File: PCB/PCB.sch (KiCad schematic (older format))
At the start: 32 parts, among them J1 USB_B, U1 ESP32-WROOM-32, X1 12MHz

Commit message: LED indicator #4
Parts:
- added Power, RXD, TXD, signal: LED_R, symbol Device:LED
- added R6, R7, R8, R9: 1k, Mlab_R:SMD-1206, symbol Device:R_Small
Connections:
- net +3V3: now also R6.2, R7.2, R8.2
- net GND: now also Power.1 (K), signal.1 (K)
- net RXD: now also RXD.1 (K)
- net TXD: now also TXD.1 (K)
- net s_LED: now reaches U1.8 (IO32)
- net s_LED: now also R9.2
- new net: R6.1, RXD.2 (A)
- new net: R7.1, TXD.2 (A)
- new net: Power.2 (A), R8.1
- new net: R9.1, signal.2 (A)
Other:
- note added: "LED"

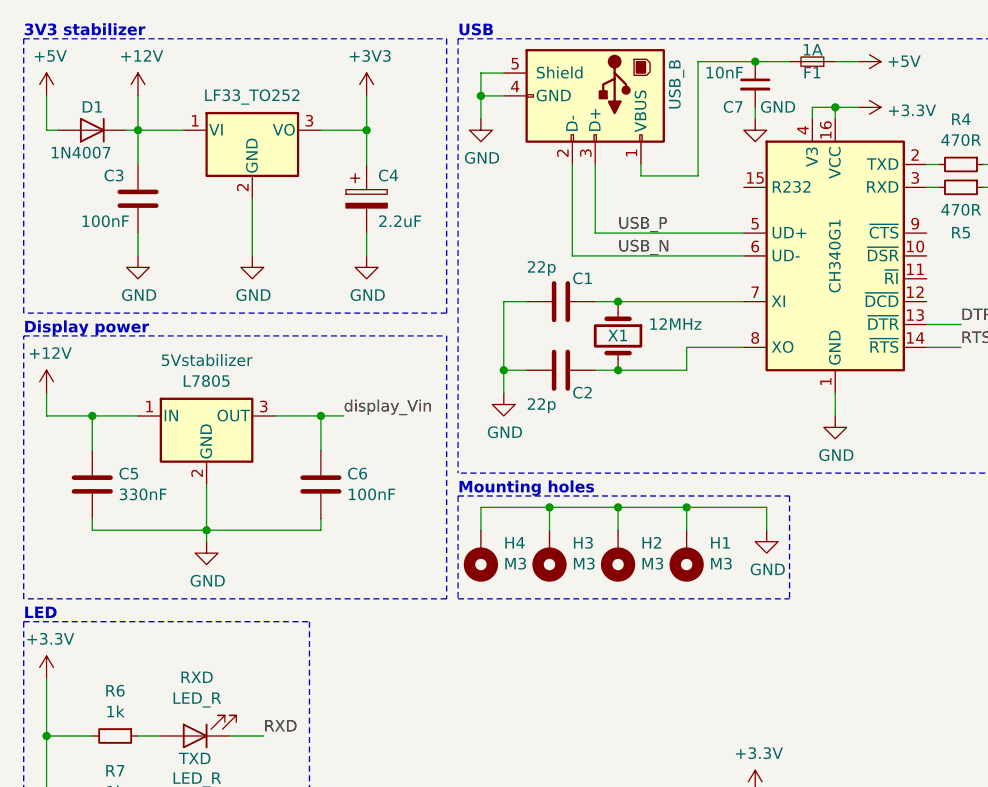
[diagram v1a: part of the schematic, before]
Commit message: schema update #4
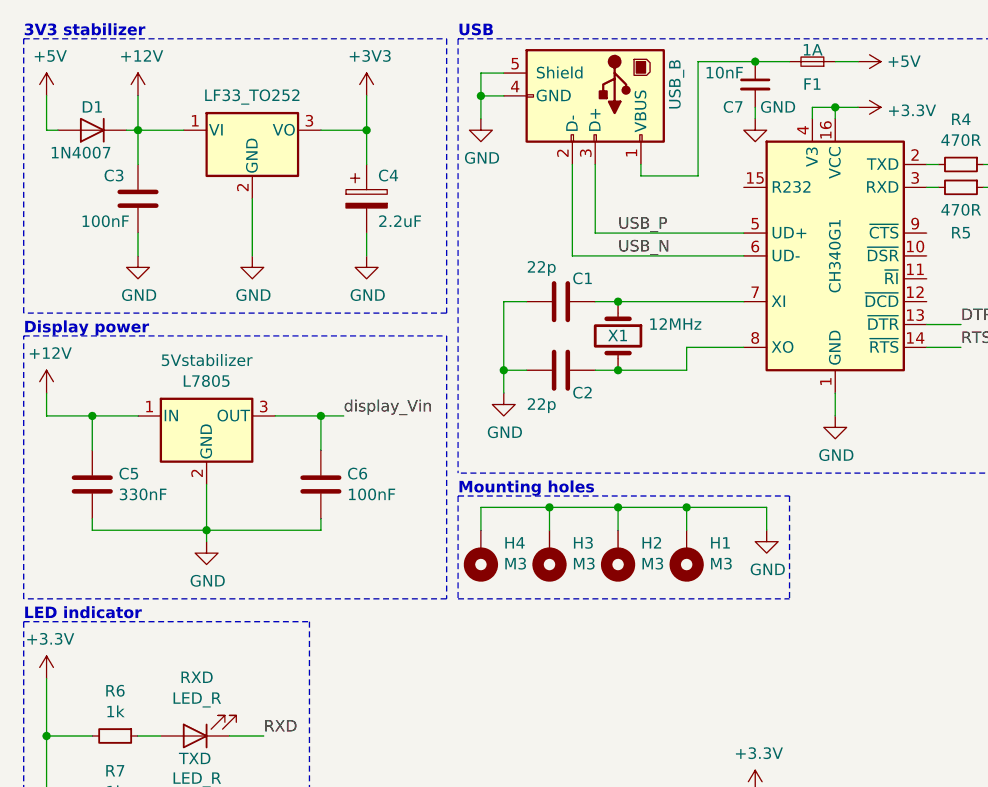
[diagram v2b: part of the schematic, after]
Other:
- note added: "LED indicator"
- note removed: "LED"
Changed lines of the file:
@@
 U 1 1 5DF6469B
 P 4000 700
-F 0 "F1" H 4000 750 50  0000 C CNN
+F 0 "F1" H 4000 800 50  0000 C CNN
 F 1 "1A" H 4000 650 50  0000 C CNN
 F 2 "Fuse:Fuse_1812_4532Metric_Pad1.30x3.40mm_HandSolder" H 4000 700 50  0001 C CNN
@@
 	550  5150 550  3150
 Text Notes 550  3150 0    50   ~ 10
-LED
+LED indicator
 $EndSCHEMATC

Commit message: reset circuit update
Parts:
- added MODE, RESET: SW_Push, symbol Switch:SW_Push
- added Q1, Q2: S8050, TO_SOT_Packages_SMD:SOT-23, symbol Transistor_BJT:S8050
- added R10, R11: 12k, symbol Device:R_Small
- added R12, R13: 10k, symbol Device:R_Small
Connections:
- net +3V3: now also R12.1, R13.1
- net GND: now also MODE.2, RESET.2
- net DTR: no longer names the net of CH340G1.13 (~DTR)
- net DTR: now also Q2.1 (E), R10.2; no longer U1.25 (IO0)
- net RTS: no longer names the net of CH340G1.14 (~RTS)
- net RTS: now also Q1.1 (E), R11.2; no longer U1.3 (EN)
- new net: Q1.2 (B), R10.1
- new net: Q2.2 (B), R11.1
- new net EN: Q1.3 (C), R12.2, RESET.1, U1.3 (EN)
- new net IO_0: MODE.1, Q2.3 (C), R13.2, U1.25 (IO0)
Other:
- note added: "Buttons"
- moved on the sheet: C1, C2, C7, CH340G1, D2, F1, H1, H2, H3, H4, I2C, NEXTION_UART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

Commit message: logo added #4
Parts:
- MODE, RESET: footprint (none) -> Buttons_Switches_SMD:SW_SPST_KMR2
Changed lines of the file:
@@
 F 0 "RESET" H 1050 6493 50  0000 C CNN
 F 1 "SW_Push" H 1050 6494 50  0001 C CNN
-F 2 "" H 1050 6500 50  0001 C CNN
+F 2 "Buttons_Switches_SMD:SW_SPST_KMR2" H 1050 6500 50  0001 C CNN
 F 3 "~" H 1050 6500 50  0001 C CNN
 	1    1050 6300
@@
 F 0 "MODE" H 1050 6793 50  0000 C CNN
 F 1 "SW_Push" H 1050 6794 50  0001 C CNN
-F 2 "" H 1050 6800 50  0001 C CNN
+F 2 "Buttons_Switches_SMD:SW_SPST_KMR2" H 1050 6800 50  0001 C CNN
 F 3 "~" H 1050 6800 50  0001 C CNN
 	1    1050 6600

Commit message: mosfet added #4
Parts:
- added P3A+, P3A-, P3B+, P3B-: WAGO256, Mlab_CON:WAGO256, symbol Connector_Generic:Conn_01x01
- added peltier3A, peltier3B: IRLR2905, Package_TO_SOT_SMD:TO-252-2_TabPin1, symbol Transistor_FET:IRLZ44N
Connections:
- net GND: now also P3A-.1 (Pin_1), P3B-.1 (Pin_1), peltier3A.3 (S), peltier3B.3 (S)
- net P3A: now reaches U1.30 (IO18)
- net P3A: now also peltier3A.1 (G)
- net P3B: now reaches U1.31 (IO19)
- net P3B: now also peltier3B.1 (G)
- new net: P3A+.1 (Pin_1), peltier3A.2 (D)
- new net: P3B+.1 (Pin_1), peltier3B.2 (D)
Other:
- note added: "3V peltiers"
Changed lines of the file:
@@
 Text Notes 550  6050 0    50   ~ 10
 Buttons
+$Comp
+L Transistor_FET:IRLZ44N peltier3A
+U 1 1 5DFD1541
+P 10200 4600
+F 0 "peltier3A" H 10406 4646 50  0000 L CNN
+F 1 "IRLR2905" H 10406 4555 50  0000 L CNN
+F 2 "Package_TO_SOT_SMD:TO-252-2_TabPin1" H 10450 4525 50  0001 L CIN
+F 3 "http://www.irf.com/product-info/datasheets/data/irlz44n.pdf" H 10200 4600 50  0001 L CNN
+	1    10200 4600
+	1    0    0    -1
+$EndComp
+$Comp
+L Connector_Generic:Conn_01x01 P3A+
+U 1 1 5DFED397
+P 10500 4300
+F 0 "P3A+" H 10580 4342 50  0000 L CNN
+F 1 "WAGO256" H 10580 4251 50  0000 L CNN
+F 2 "Mlab_CON:WAGO256" H 10500 4300 50  0001 C CNN
+F 3 "~" H 10500 4300 50  0001 C CNN
+	1    10500 4300
+	1    0    0    -1
+$EndComp
+$Comp
+L Connector_Generic:Conn_01x01 P3A-
+U 1 1 5DFF358D
+P 10500 4900
+F 0 "P3A-" H 10580 4942 50  0000 L CNN
+F 1 "WAGO256" H 10580 4851 50  0000 L CNN
+F 2 "Mlab_CON:WAGO256" H 10500 4900 50  0001 C CNN
+F 3 "~" H 10500 4900 50  0001 C CNN
+	1    10500 4900
+	1    0    0    -1
+$EndComp
+$Comp
+L power:GND #PWR?
+U 1 1 5E01ED3C
+P 10300 5000
+F 0 "#PWR?" H 10300 4750 50  0001 C CNN
+F 1 "GND" H 10305 4827 50  0000 C CNN
+F 2 "" H 10300 5000 50  0001 C CNN
+F 3 "" H 10300 5000 50  0001 C CNN
+	1    10300 5000
+	1    0    0    -1
+$EndComp
+Wire Wire Line
+	10300 4800 10300 4900
+Connection ~ 10300 4900
+Wire Wire Line
+	10300 4900 10300 5000
+Wire Wire Line
+	10300 4300 10300 4400
+Wire Wire Line
+	10000 4600 9950 4600
+Wire Wire Line
+	4350 5450 4500 5450
+Text Label 9950 4600 2    50   ~ 0
+P3A
+Text Label 4500 5450 0    50   ~ 0
+P3A
+$Comp
+L Transistor_FET:IRLZ44N peltier3B
+U 1 1 5E0B6BCD
+P 10200 5650
+F 0 "peltier3B" H 10406 5696 50  0000 L CNN
+F 1 "IRLR2905" H 10406 5605 50  0000 L CNN
+F 2 "Package_TO_SOT_SMD:TO-252-2_TabPin1" H 10450 5575 50  0001 L CIN
+F 3 "http://www.irf.com/product-info/datasheets/data/irlz44n.pdf" H 10200 5650 50  0001 L CNN
+	1    10200 5650
+	1    0    0    -1
+$EndComp
+$Comp
+L Connector_Generic:Conn_01x01 P3B+
+U 1 1 5E0B6BD7
+P 10500 5350
+F 0 "P3B+" H 10580 5392 50  0000 L CNN
+F 1 "WAGO256" H 10580 5301 50  0000 L CNN
+F 2 "Mlab_CON:WAGO256" H 10500 5350 50  0001 C CNN
+F 3 "~" H 10500 5350 50  0001 C CNN
+	1    10500 5350
+	1    0    0    -1
+$EndComp
+$Comp
+L Connector_Generic:Conn_01x01 P3B-
+U 1 1 5E0B6BE1
+P 10500 5950
+F 0 "P3B-" H 10580 5992 50  0000 L CNN
+F 1 "WAGO256" H 10580 5901 50  0000 L CNN
+F 2 "Mlab_CON:WAGO256" H 10500 5950 50  0001 C CNN
+F 3 "~" H 10500 5950 50  0001 C CNN
+	1    10500 5950
+	1    0    0    -1
+$EndComp
+$Comp
+L power:GND #PWR?
+U 1 1 5E0B6BEB
+P 10300 6050
+F 0 "#PWR?" H 10300 5800 50  0001 C CNN
+F 1 "GND" H 10305 5877 50  0000 C CNN
+F 2 "" H 10300 6050 50  0001 C CNN
+F 3 "" H 10300 6050 50  0001 C CNN
+	1    10300 6050
+	1    0    0    -1
+$EndComp
+Wire Wire Line
+	10300 5850 10300 5950
+Connection ~ 10300 5950
+Wire Wire Line
+	10300 5950 10300 6050
+Wire Wire Line
+	10300 5350 10300 5450
+Wire Wire Line
+	10000 5650 9950 5650
+Text Label 9950 5650 2    50   ~ 0
+P3B
+Wire Wire Line
+	4350 5550 4500 5550
+Text Label 4500 5550 0    50   ~ 0
+P3B
+Wire Notes Line
+	9800 6300 9800 4200
+Wire Notes Line
+	9800 4200 10950 4200
+Wire Notes Line
+	10950 4200 10950 6300
+Wire Notes Line
+	9800 6300 10950 6300
+Text Notes 9800 4200 0    50   ~ 10
+3V peltiers
 $EndSCHEMATC

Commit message: peltiers #4
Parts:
- added P12A+, P12A-, P12B+, P12B-: WAGO256, Mlab_CON:WAGO256, symbol Connector_Generic:Conn_01x01
- added peltier12A, peltier12B: IRLR2905, Package_TO_SOT_SMD:TO-252-2_TabPin1, symbol Transistor_FET:IRLZ44N
- renumbered 3V3stabilizer to 3V3stabilizer1, 5Vstabilizer to 5Vstabilizer1, I2C to I2C1, MODE to MODE1, NEXTION_UART to NEXTION_UART1, OneWire to OneWire1, Power to Power1, RESET to RESET1, RXD to RXD1, TXD to TXD1, peltier3A to peltier3A1, peltier3B to peltier3B1, power12V to power12V1, signal to signal1
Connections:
- net GND: now also P12A-.1 (Pin_1), P12B-.1 (Pin_1), peltier12A.3 (S), peltier12B.3 (S)
- net P12A: now reaches U1.33 (IO21)
- net P12A: now also peltier12A.1 (G)
- net P12B: now reaches U1.36 (IO22)
- net P12B: now also peltier12B.1 (G)
- new net: P12A+.1 (Pin_1), peltier12A.2 (D)
- new net: P12B+.1 (Pin_1), peltier12B.2 (D)
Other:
- note added: "12V peltiers"
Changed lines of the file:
@@
 $EndComp
 $Comp
-L Connector_Generic:Conn_01x04 power12V
+L Connector_Generic:Conn_01x04 power12V1
 U 1 1 5DEF05BC
 P 9800 700
-F 0 "power12V" V 9800 400 50  0000 R CNN
+F 0 "power12V1" V 9800 400 50  0000 R CNN
 F 1 "Conn_01x04" V 9700 400 50  0001 R CNN
 F 2 "Mlab_Pin_Headers:Straight_2x04" H 9800 700 50  0001 C CNN
@@
 $EndComp
 $Comp
-L Regulator_Linear:LF33_TO252 3V3stabilizer
+L Regulator_Linear:LF33_TO252 3V3stabilizer1
 U 1 1 5DEEC619
 P 1550 1000
-F 0 "3V3stabilizer" H 1550 1242 50  0001 C CNN
+F 0 "3V3stabilizer1" H 1550 1242 50  0001 C CNN
 F 1 "LF33_TO252" H 1550 1151 50  0000 C CNN
 F 2 "Package_TO_SOT_SMD:TO-252-2" H 1550 1225 50  0001 C CIN
@@
 	10800 1400 9600 1400
 $Comp
-L Regulator_Linear:L7805 5Vstabilizer
+L Regulator_Linear:L7805 5Vstabilizer1
 U 1 1 5DEFDF14
 P 1350 2250
-F 0 "5Vstabilizer" H 1350 2492 50  0000 C CNN
+F 0 "5Vstabilizer1" H 1350 2492 50  0000 C CNN
 F 1 "L7805" H 1350 2401 50  0000 C CNN
 F 2 "Package_TO_SOT_SMD:TO-252-2" H 1375 2100 50  0001 L CIN
@@
 U2_TXD
 $Comp
-L Connector_Generic:Conn_01x05 I2C
+L Connector_Generic:Conn_01x05 I2C1
 U 1 1 5E001ADA
 P 8100 750
-F 0 "I2C" V 8200 800 50  0000 R CNN
+F 0 "I2C1" V 8200 800 50  0000 R CNN
 F 1 "Conn_01x05" V 7973 462 50  0001 R CNN
 F 2 "Mlab_Pin_Headers:Straight_2x05" H 8100 750 50  0001 C CNN
@@
 I2C
 $Comp
-L Connector_Generic:Conn_01x04 NEXTION_UART
+L Connector_Generic:Conn_01x04 NEXTION_UART1
 U 1 1 5E06DABD
 P 800 5400
-F 0 "NEXTION_UART" V 900 5600 50  0000 R CNN
+F 0 "NEXTION_UART1" V 900 5600 50  0000 R CNN
 F 1 "Conn_01x04" V 673 5112 50  0001 R CNN
 F 2 "Mlab_Pin_Headers:Angled_1x04" H 800 5400 50  0001 C CNN
@@
 OneWire
 $Comp
-L Connector_Generic:Conn_01x05 OneWire
+L Connector_Generic:Conn_01x05 OneWire1
 U 1 1 5E31DD38
 P 9100 750
-F 0 "OneWire" V 9200 900 50  0000 R CNN
+F 0 "OneWire1" V 9200 900 50  0000 R CNN
 F 1 "Conn_01x05" V 8973 462 50  0001 R CNN
 F 2 "Mlab_Pin_Headers:Straight_2x05" H 9100 750 50  0001 C CNN
@@
 	7300 1950 7300 2400
 $Comp
-L Device:LED RXD
+L Device:LED RXD1
 U 1 1 5E04BA83
 P 1300 3650
-F 0 "RXD" H 1293 3395 50  0000 C CNN
+F 0 "RXD1" H 1293 3395 50  0000 C CNN
 F 1 "LED_R" H 1293 3486 50  0000 C CNN
 F 2 "" H 1300 3650 50  0001 C CNN
@@
 $EndComp
 $Comp
-L power:+3.3V #PWR?
+L power:+3.3V #PWR0136
 U 1 1 5E061ED7
 P 650 3400
-F 0 "#PWR?" H 650 3250 50  0001 C CNN
+F 0 "#PWR0136" H 650 3250 50  0001 C CNN
 F 1 "+3.3V" H 665 3573 50  0000 C CNN
 F 2 "" H 650 3400 50  0001 C CNN
@@
 $EndComp
 $Comp
-L Device:LED TXD
+L Device:LED TXD1
 U 1 1 5E062710
 P 1300 4000
-F 0 "TXD" H 1300 3750 50  0000 C CNN
+F 0 "TXD1" H 1300 3750 50  0000 C CNN
 F 1 "LED_R" H 1293 3836 50  0000 C CNN
 F 2 "" H 1300 4000 50  0001 C CNN
@@
 TXD
 $Comp
-L Device:LED Power
+L Device:LED Power1
 U 1 1 5E08E5BB
 P 1300 4400
-F 0 "Power" H 1300 4150 50  0000 C CNN
+F 0 "Power1" H 1300 4150 50  0000 C CNN
 F 1 "LED_R" H 1293 4236 50  0000 C CNN
 F 2 "" H 1300 4400 50  0001 C CNN
@@
 $EndComp
 $Comp
-L Device:LED signal
+L Device:LED signal1
 U 1 1 5E08F438
 P 1300 4800
-F 0 "signal" H 1300 4550 50  0000 C CNN
+F 0 "signal1" H 1300 4550 50  0000 C CNN
 F 1 "LED_R" H 1293 4636 50  0000 C CNN
 F 2 "" H 1300 4800 50  0001 C CNN
@@
 Connection ~ 650  4000
 $Comp
-L power:GND #PWR?
+L power:GND #PWR0137
 U 1 1 5E09628C
 P 1600 4900
-F 0 "#PWR?" H 1600 4650 50  0001 C CNN
+F 0 "#PWR0137" H 1600 4650 50  0001 C CNN
 F 1 "GND" H 1605 4727 50  0000 C CNN
 F 2 "" H 1600 4900 50  0001 C CNN
@@
 IO_0
 $Comp
-L power:+3.3V #PWR?
+L power:+3.3V #PWR0138
 U 1 1 5E0DC59F
 P 5150 950
-F 0 "#PWR?" H 5150 800 50  0001 C CNN
+F 0 "#PWR0138" H 5150 800 50  0001 C CNN
 F 1 "+3.3V" H 5165 1123 50  0000 C CNN
 F 2 "" H 5150 950 50  0001 C CNN
@@
 $EndComp
 $Comp
-L power:+3.3V #PWR?
+L power:+3.3V #PWR0139
 U 1 1 5E0F42C2
 P 5400 950
-F 0 "#PWR?" H 5400 800 50  0001 C CNN
+F 0 "#PWR0139" H 5400 800 50  0001 C CNN
 F 1 "+3.3V" H 5415 1123 50  0000 C CNN
 F 2 "" H 5400 950 50  0001 C CNN
@@
 EN
 $Comp
-L power:GND #PWR?
+L power:GND #PWR0140
 U 1 1 5E153620
 P 1350 6300
-F 0 "#PWR?" H 1350 6050 50  0001 C CNN
+F 0 "#PWR0140" H 1350 6050 50  0001 C CNN
 F 1 "GND" H 1355 6127 50  0000 C CNN
 F 2 "" H 1350 6300 50  0001 C CNN
@@
 	1250 6300 1350 6300
 $Comp
-L Switch:SW_Push RESET
+L Switch:SW_Push RESET1
 U 1 1 5E140153
 P 1050 6300
-F 0 "RESET" H 1050 6493 50  0000 C CNN
+F 0 "RESET1" H 1050 6493 50  0000 C CNN
 F 1 "SW_Push" H 1050 6494 50  0001 C CNN
 F 2 "Buttons_Switches_SMD:SW_SPST_KMR2" H 1050 6500 50  0001 C CNN
@@
 IO_0
 $Comp
-L power:GND #PWR?
+L power:GND #PWR0141
 U 1 1 5E1870BD
 P 1350 6600
-F 0 "#PWR?" H 1350 6350 50  0001 C CNN
+F 0 "#PWR0141" H 1350 6350 50  0001 C CNN
 F 1 "GND" H 1355 6427 50  0000 C CNN
 F 2 "" H 1350 6600 50  0001 C CNN
@@
 	1250 6600 1350 6600
 $Comp
-L Switch:SW_Push MODE
+L Switch:SW_Push MODE1
 U 1 1 5E1870C9
 P 1050 6600
-F 0 "MODE" H 1050 6793 50  0000 C CNN
+F 0 "MODE1" H 1050 6793 50  0000 C CNN
 F 1 "SW_Push" H 1050 6794 50  0001 C CNN
 F 2 "Buttons_Switches_SMD:SW_SPST_KMR2" H 1050 6800 50  0001 C CNN
@@
 Buttons
 $Comp
-L Transistor_FET:IRLZ44N peltier3A
+L Transistor_FET:IRLZ44N peltier3A1
 U 1 1 5DFD1541
 P 10200 4600
-F 0 "peltier3A" H 10406 4646 50  0000 L CNN
+F 0 "peltier3A1" H 10406 4646 50  0000 L CNN
 F 1 "IRLR2905" H 10406 4555 50  0000 L CNN
 F 2 "Package_TO_SOT_SMD:TO-252-2_TabPin1" H 10450 4525 50  0001 L CIN
@@
 $EndComp
 $Comp
-L power:GND #PWR?
+L power:GND #PWR0142
 U 1 1 5E01ED3C
 P 10300 5000
-F 0 "#PWR?" H 10300 4750 50  0001 C CNN
+F 0 "#PWR0142" H 10300 4750 50  0001 C CNN
 F 1 "GND" H 10305 4827 50  0000 C CNN
 F 2 "" H 10300 5000 50  0001 C CNN
@@
 P3A
 $Comp
-L Transistor_FET:IRLZ44N peltier3B
+L Transistor_FET:IRLZ44N peltier3B1
 U 1 1 5E0B6BCD
 P 10200 5650
-F 0 "peltier3B" H 10406 5696 50  0000 L CNN
+F 0 "peltier3B1" H 10406 5696 50  0000 L CNN
 F 1 "IRLR2905" H 10406 5605 50  0000 L CNN
 F 2 "Package_TO_SOT_SMD:TO-252-2_TabPin1" H 10450 5575 50  0001 L CIN
@@
 $EndComp
 $Comp
-L power:GND #PWR?
+L power:GND #PWR0143
 U 1 1 5E0B6BEB
 P 10300 6050
-F 0 "#PWR?" H 10300 5800 50  0001 C CNN
+F 0 "#PWR0143" H 10300 5800 50  0001 C CNN
 F 1 "GND" H 10305 5877 50  0000 C CNN
 F 2 "" H 10300 6050 50  0001 C CNN
@@
 P3B
 Wire Notes Line
-	9800 6300 9800 4200
-Wire Notes Line
-	9800 4200 10950 4200
+	9750 6300 9750 4200
 Wire Notes Line
 	10950 4200 10950 6300
-Wire Notes Line
-	9800 6300 10950 6300
-Text Notes 9800 4200 0    50   ~ 10
+Text Notes 9750 4200 0    50   ~ 10
 3V peltiers
+$Comp
+L Transistor_FET:IRLZ44N peltier12A
+U 1 1 5E1B3091
+P 10200 2400
+F 0 "peltier12A" H 10406 2446 50  0000 L CNN
+F 1 "IRLR2905" H 10406 2355 50  0000 L CNN
+F 2 "Package_TO_SOT_SMD:TO-252-2_TabPin1" H 10450 2325 50  0001 L CIN
+F 3 "http://www.irf.com/product-info/datasheets/data/irlz44n.pdf" H 10200 2400 50  0001 L CNN
+	1    10200 2400
+	1    0    0    -1
+$EndComp
+$Comp
+L Connector_Generic:Conn_01x01 P12A+
+U 1 1 5E1B309B
+P 10500 2100
+F 0 "P12A+" H 10580 2142 50  0000 L CNN
+F 1 "WAGO256" H 10580 2051 50  0000 L CNN
+F 2 "Mlab_CON:WAGO256" H 10500 2100 50  0001 C CNN
+F 3 "~" H 10500 2100 50  0001 C CNN
+	1    10500 2100
+	1    0    0    -1
+$EndComp
+$Comp
+L Connector_Generic:Conn_01x01 P12A-
+U 1 1 5E1B30A5
+P 10500 2700
+F 0 "P12A-" H 10580 2742 50  0000 L CNN
+F 1 "WAGO256" H 10580 2651 50  0000 L CNN
+F 2 "Mlab_CON:WAGO256" H 10500 2700 50  0001 C CNN
+F 3 "~" H 10500 2700 50  0001 C CNN
+	1    10500 2700
+	1    0    0    -1
+$EndComp
+$Comp
+L power:GND #PWR?
+U 1 1 5E1B30AF
+P 10300 2800
+F 0 "#PWR?" H 10300 2550 50  0001 C CNN
+F 1 "GND" H 10305 2627 50  0000 C CNN
+F 2 "" H 10300 2800 50  0001 C CNN
+F 3 "" H 10300 2800 50  0001 C CNN
+	1    10300 2800
+	1    0    0    -1
+$EndComp
+Wire Wire Line
+	10300 2600 10300 2700
+Connection ~ 10300 2700
+Wire Wire Line
+	10300 2700 10300 2800
+Wire Wire Line
+	10300 2100 10300 2200
+Wire Wire Line
+	10000 2400 9950 2400
+Text Label 9950 2400 2    50   ~ 0
+P12A
+$Comp
+L Transistor_FET:IRLZ44N peltier12B
+U 1 1 5E1B30BF
+P 10200 3450
+F 0 "peltier12B" H 10406 3496 50  0000 L CNN
+F 1 "IRLR2905" H 10406 3405 50  0000 L CNN
+F 2 "Package_TO_SOT_SMD:TO-252-2_TabPin1" H 10450 3375 50  0001 L CIN
+F 3 "http://www.irf.com/product-info/datasheets/data/irlz44n.pdf" H 10200 3450 50  0001 L CNN
+	1    10200 3450
+	1    0    0    -1
+$EndComp
+$Comp
+L Connector_Generic:Conn_01x01 P12B+
+U 1 1 5E1B30C9
+P 10500 3150
+F 0 "P12B+" H 10580 3192 50  0000 L CNN
+F 1 "WAGO256" H 10580 3101 50  0000 L CNN
+F 2 "Mlab_CON:WAGO256" H 10500 3150 50  0001 C CNN
+F 3 "~" H 10500 3150 50  0001 C CNN
+	1    10500 3150
+	1    0    0    -1
+$EndComp
+$Comp
+L Connector_Generic:Conn_01x01 P12B-
+U 1 1 5E1B30D3
+P 10500 3750
+F 0 "P12B-" H 10580 3792 50  0000 L CNN
+F 1 "WAGO256" H 10580 3701 50  0000 L CNN
+F 2 "Mlab_CON:WAGO256" H 10500 3750 50  0001 C CNN
+F 3 "~" H 10500 3750 50  0001 C CNN
+	1    10500 3750
+	1    0    0    -1
+$EndComp
+$Comp
+L power:GND #PWR?
+U 1 1 5E1B30DD
+P 10300 3850
+F 0 "#PWR?" H 10300 3600 50  0001 C CNN
+F 1 "GND" H 10305 3677 50  0000 C CNN
+F 2 "" H 10300 3850 50  0001 C CNN
+F 3 "" H 10300 3850 50  0001 C CNN
+	1    10300 3850
+	1    0    0    -1
+$EndComp
+Wire Wire Line
+	10300 3650 10300 3750
+Connection ~ 10300 3750
+Wire Wire Line
+	10300 3750 10300 3850
+Wire Wire Line
+	10300 3150 10300 3250
+Wire Wire Line
+	10000 3450 9950 3450
+Text Label 9950 3450 2    50   ~ 0
+P12B
+Wire Notes Line
+	9750 4100 9750 2000
+Wire Notes Line
+	10950 2000 10950 4100
+Text Notes 9750 2000 0    50   ~ 10
+12V peltiers
+Wire Notes Line
+	9750 4100 10950 4100
+Wire Notes Line
+	9750 2000 10950 2000
+Wire Notes Line
+	9750 6300 10950 6300
+Wire Notes Line
+	9750 4200 10950 4200
+Wire Wire Line
+	4350 5650 4500 5650
+Wire Wire Line
+	4350 5750 4500 5750
+Text Label 4500 5650 0    50   ~ 0
+P12A
+Text Label 4500 5750 0    50   ~ 0
+P12B
 $EndSCHEMATC
